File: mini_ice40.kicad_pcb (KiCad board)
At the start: 2 copper layers, 3 parts, among them P1 Pin_Header_Straight_1x18, P2 Pin_Header_Straight_1x18

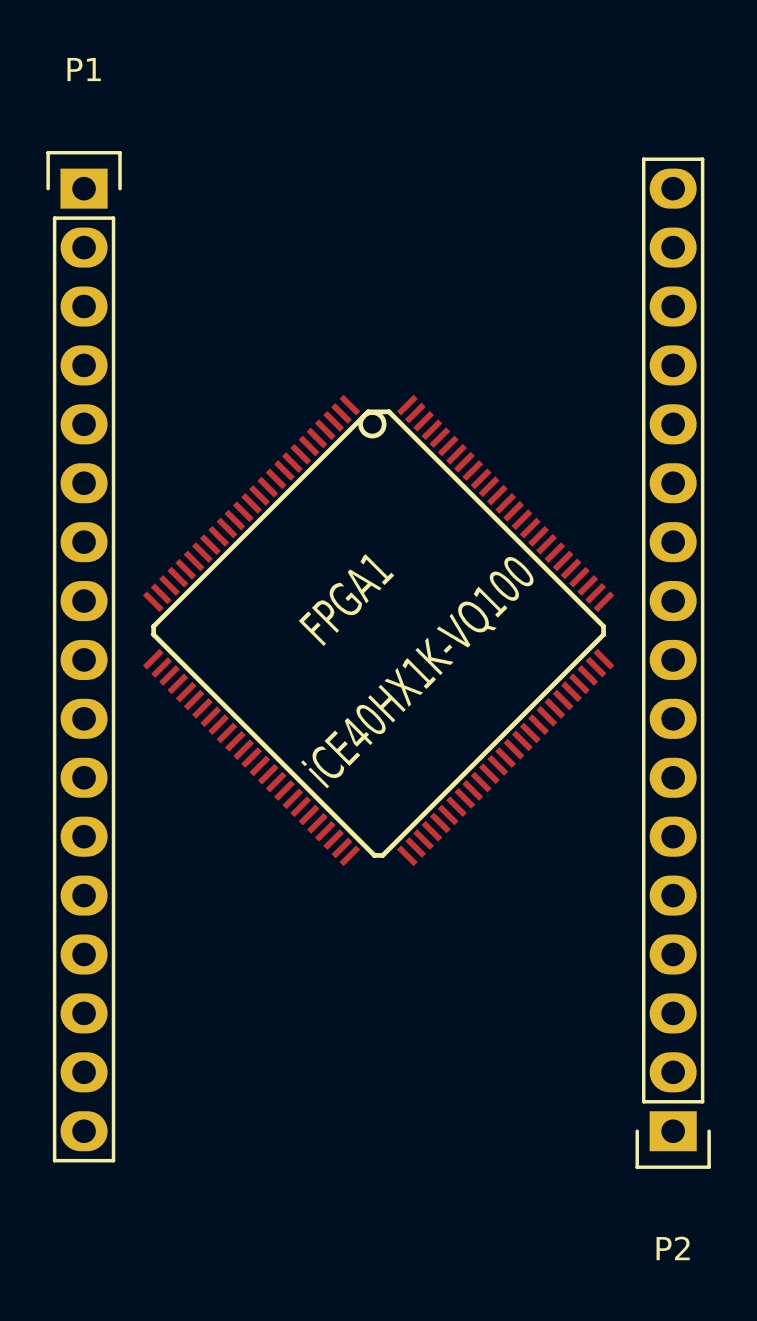
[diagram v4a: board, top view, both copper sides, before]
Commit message: ** 4-layer PCB design
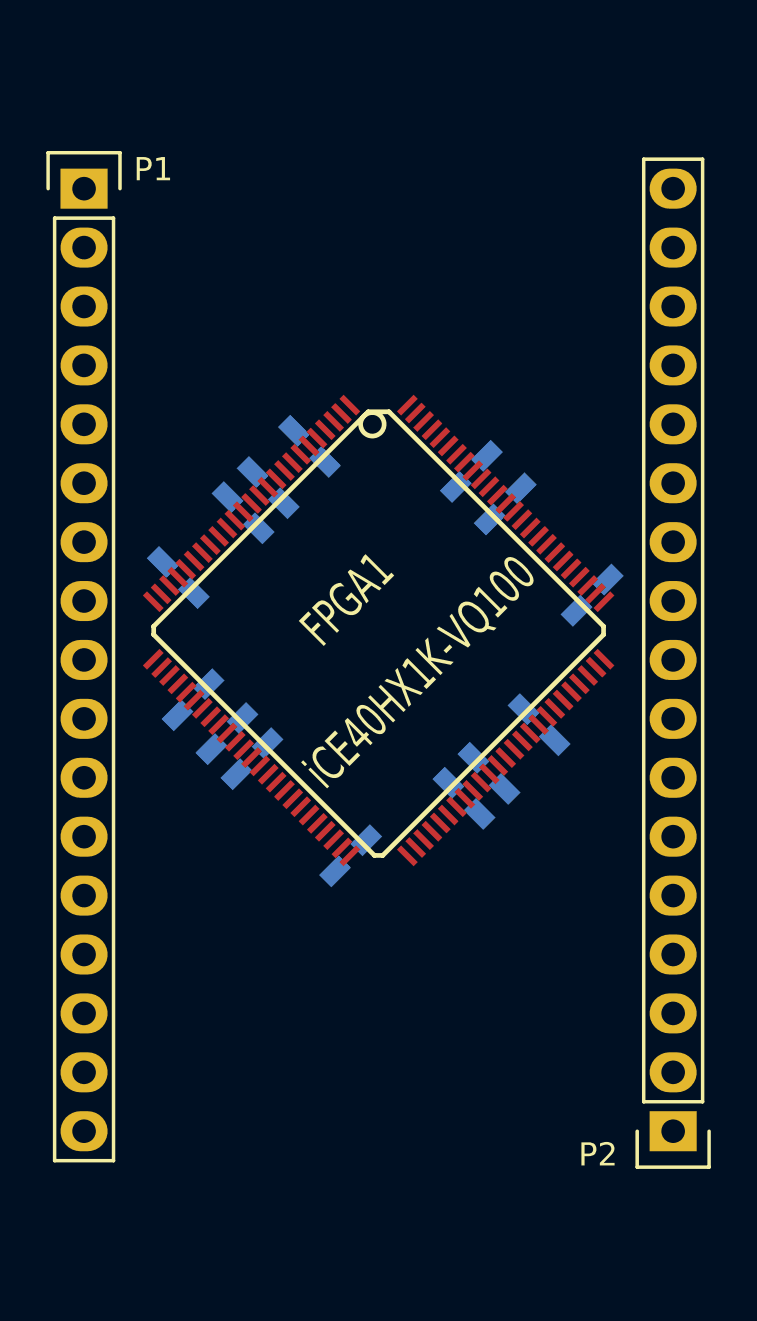
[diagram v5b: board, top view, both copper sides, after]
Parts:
- added C10: C_0603_HandSoldering, Capacitors_SMD:C_0603_HandSoldering, B.Cu at (22.5, 39.8)
- added C11: C_0603_HandSoldering, Capacitors_SMD:C_0603_HandSoldering, B.Cu at (26.7, 44.0)
- added C12: C_0603_HandSoldering, Capacitors_SMD:C_0603_HandSoldering, B.Cu at (31.6, 41.5)
- added C13: C_0603_HandSoldering, Capacitors_SMD:C_0603_HandSoldering, B.Cu at (34.9, 38.4)
- added C14: C_0603_HandSoldering, Capacitors_SMD:C_0603_HandSoldering, B.Cu at (33.4, 28.8)
- added C15: C_0603_HandSoldering, Capacitors_SMD:C_0603_HandSoldering, B.Cu at (31.9, 27.4)
- added C16: C_0603_HandSoldering, Capacitors_SMD:C_0603_HandSoldering, B.Cu at (23.2, 28.1)
- added C17: C_0603_HandSoldering, Capacitors_SMD:C_0603_HandSoldering, B.Cu at (21.4, 38.7)
- added C18: C_0603_HandSoldering, Capacitors_SMD:C_0603_HandSoldering, B.Cu at (32.7, 40.4)
- added C19: C_0603_HandSoldering, Capacitors_SMD:C_0603_HandSoldering, B.Cu at (37.1, 32.8)
- added C6: C_0603_HandSoldering, Capacitors_SMD:C_0603_HandSoldering, B.Cu at (25.0, 26.4)
- added C7: C_0603_HandSoldering, Capacitors_SMD:C_0603_HandSoldering, B.Cu at (22.1, 29.2)
- added C8: C_0603_HandSoldering, Capacitors_SMD:C_0603_HandSoldering, B.Cu at (19.3, 32.0)
- added C9: C_0603_HandSoldering, Capacitors_SMD:C_0603_HandSoldering, B.Cu at (19.9, 37.3)
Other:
- copper layers 2 -> 4
- net class Default: trace_width 0.25 -> 0.2; via_dia 0.6 -> 0.5; via_drill 0.4 -> 0.3

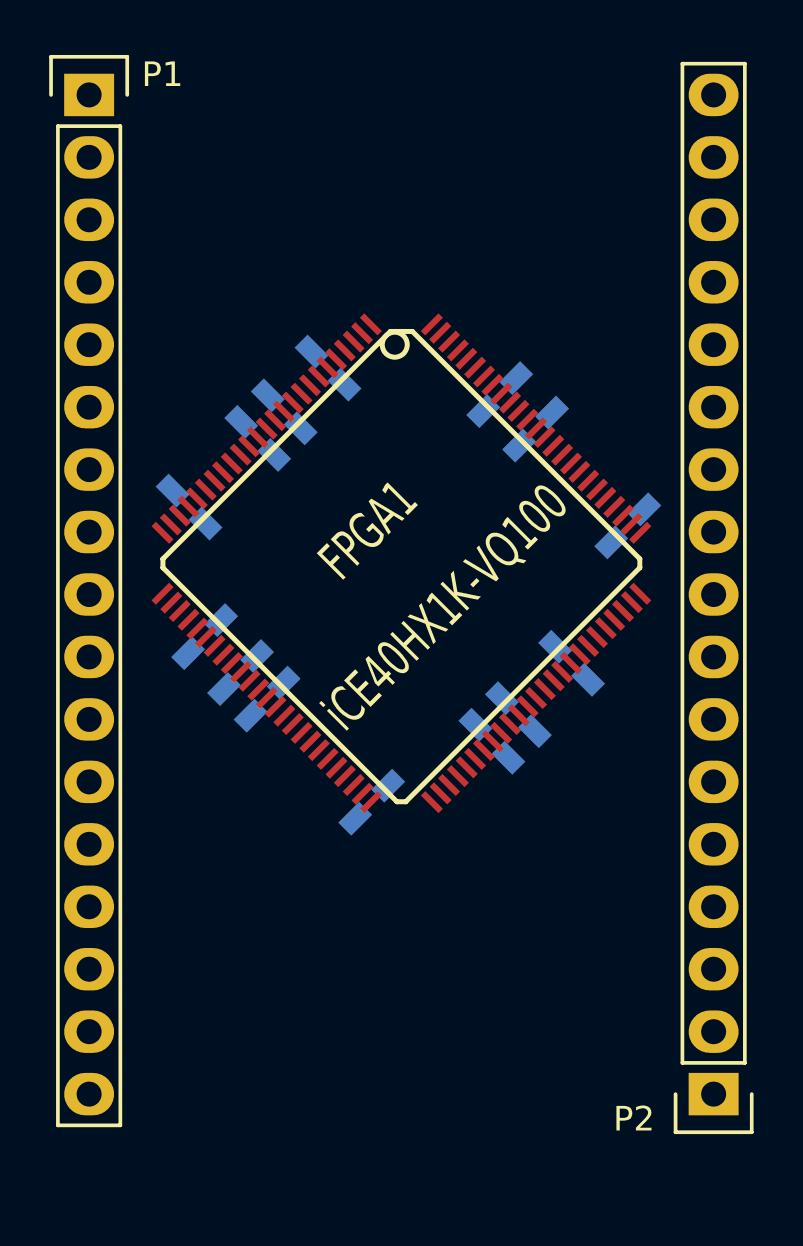
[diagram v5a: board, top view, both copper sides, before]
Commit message: ** 4-layer PCB sans GPIO
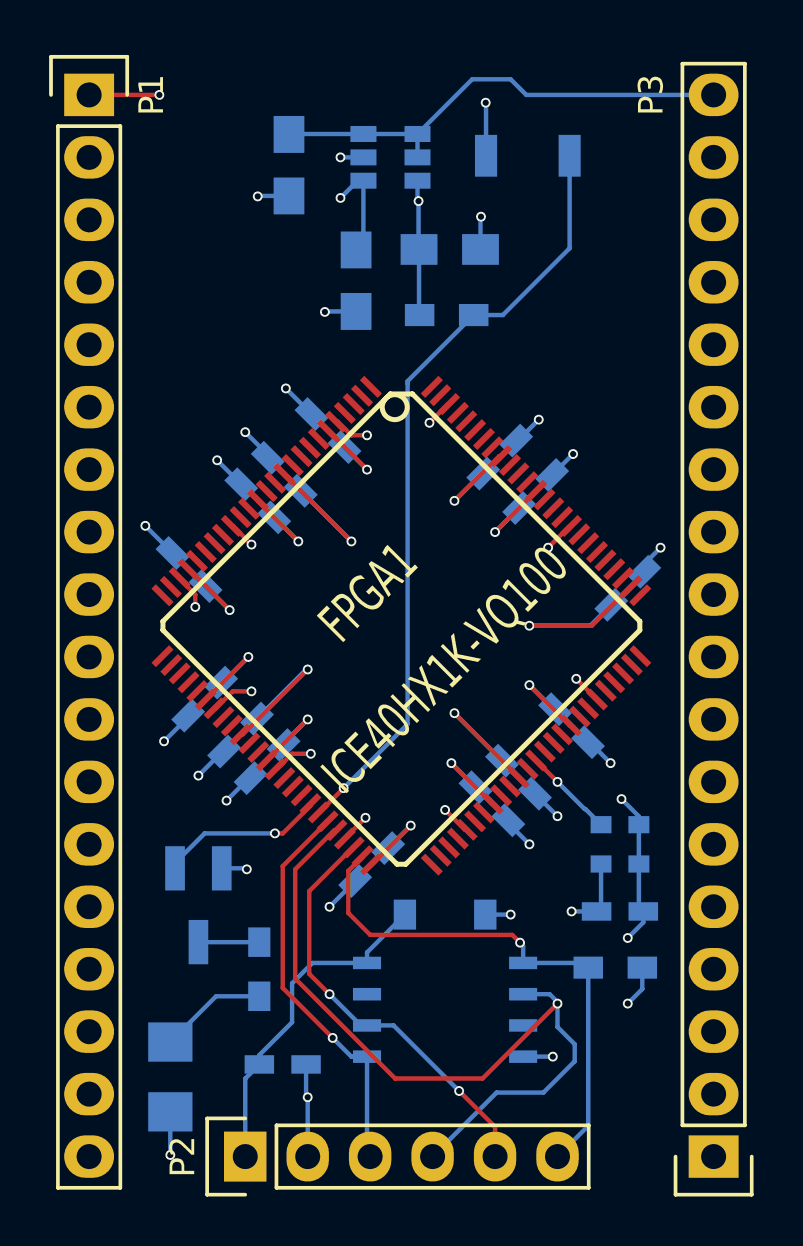
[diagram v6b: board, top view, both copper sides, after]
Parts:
- added C1: 1u, Capacitors_SMD:C_0805_HandSoldering, B.Cu at (23.4, 18.1)
- added C2: 1u, Capacitors_SMD:C_0805_HandSoldering, B.Cu at (26.1, 22.8)
- added C3: 1u, Capacitors_SMD:C_0805_HandSoldering, B.Cu at (29.9, 21.5)
- added C4: 0u1, Capacitors_SMD:C_0603_HandSoldering, B.Cu at (23.1, 54.7)
- added C5: 0u1, Capacitors_SMD:C_0603_HandSoldering, B.Cu at (36.8, 48.5)
- added D1: 1N4448WQ-7-F, Diodes_SMD:SOD-123, B.Cu at (29.7, 48.6)
- added DDONE1: SML-LX1206GC-TR1, LEDs:LED_1206, B.Cu at (18.5, 55.2)
- added OSC1: ASDMB-26MHZ-LC, mini_ice40:2MMx2MM5, B.Cu at (36.8, 45.7)
- added P3: CONN_01X18, Pin_Headers:Pin_Header_Straight_1x18, F.Cu at (40.6, 58.4)
- added Q1: 2N7002LT1G, TO_SOT_Packages_SMD:SOT-23_Handsoldering, B.Cu at (19.7, 48.2)
- added R1: 330, Resistors_SMD:R_0603_HandSoldering, B.Cu at (22.2, 50.8)
- added R2: 10K, Resistors_SMD:R_0603_HandSoldering, B.Cu at (29.8, 24.2)
- added R3: 10K, Resistors_SMD:R_0603_HandSoldering, B.Cu at (36.6, 50.7)
- added REG1: AP7312-1233W6-7, TO_SOT_Packages_SMD:SOT-23-6, B.Cu at (27.5, 17.8)
- added RST1: SW_PUSH, Buttons_Switches_SMD:SW_SPST_B3U-1000P, B.Cu at (33.1, 17.7)
- added SPI_FLASH1: AT25SF041-SSHD-B, SMD_Packages:SOIC-8-N, B.Cu at (29.7, 52.5)
- C10, C11, C12, C13, C14, C15, C16, C17, C18, C19, C6, C7, C8, C9: value C_0603_HandSoldering -> 0u1
- FPGA1: value iCE40HX1K-VQ100 -> ICE40HX1K-VQ100
- P1: value Pin_Header_Straight_1x18 -> CONN_01X18; footprint Pin_Headers:Pin_Header_Straight_1x17 -> Pin_Headers:Pin_Header_Straight_1x18
- P2: value Pin_Header_Straight_1x18 -> CONN_01X04; footprint Pin_Headers:Pin_Header_Straight_1x17 -> Pin_Headers:Pin_Header_Straight_1x06
- moved P2 19.2 mm to (21.6, 58.4), turned to 90 degrees
- moved C15 2.54 mm to (31.9, 30.0)
- moved C10 2.54 mm to (22.5, 42.4)
- moved C11 2.54 mm to (26.7, 46.5)
- moved C12 2.54 mm to (31.6, 44.1)
- moved C13 2.54 mm to (34.9, 40.9)
- moved C14 2.54 mm to (33.4, 31.4)
- moved C16 2.54 mm to (23.2, 30.7)
- moved C17 2.54 mm to (21.4, 41.3)
- moved C18 2.54 mm to (32.7, 43.0)
- moved C19 2.54 mm to (37.1, 35.3)
- moved C6 2.54 mm to (25.0, 28.9)
- moved C7 2.54 mm to (22.1, 31.8)
- moved C8 2.54 mm to (19.3, 34.5)
- moved C9 2.54 mm to (19.9, 39.8)
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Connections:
- C10 pad 1: (no net) -> +3V3
- C10 pad 2: (no net) -> GND
- C11 pad 1: (no net) -> +3V3
- C11 pad 2: (no net) -> GND
- C12 pad 1: (no net) -> +3V3
- C12 pad 2: (no net) -> GND
- C13 pad 1: (no net) -> +3V3
- C13 pad 2: (no net) -> GND
- C14 pad 1: (no net) -> +3V3
- C14 pad 2: (no net) -> GND
- C15 pad 1: (no net) -> +3V3
- C15 pad 2: (no net) -> GND
- C16 pad 1: (no net) -> +1V2
- C16 pad 2: (no net) -> GND
- C17 pad 1: (no net) -> +1V2
- C17 pad 2: (no net) -> GND
- C18 pad 1: (no net) -> +1V2
- C18 pad 2: (no net) -> GND
- C19 pad 1: (no net) -> +1V2
- C19 pad 2: (no net) -> GND
- C6 pad 1: (no net) -> +3V3
- C6 pad 2: (no net) -> GND
- C7 pad 1: (no net) -> +3V3
- C7 pad 2: (no net) -> GND
- C8 pad 1: (no net) -> +3V3
- C8 pad 2: (no net) -> GND
- C9 pad 1: (no net) -> +3V3
- C9 pad 2: (no net) -> GND
- FPGA1 pad 1: (no net) -> Net-(FPGA1-Pad1)
- FPGA1 pad 10: (no net) -> Net-(FPGA1-Pad10)
- FPGA1 pad 100: (no net) -> Net-(FPGA1-Pad100)
- FPGA1 pad 11: (no net) -> +1V2
- FPGA1 pad 12: (no net) -> Net-(FPGA1-Pad12)
- FPGA1 pad 13: (no net) -> Net-(FPGA1-Pad13)
- FPGA1 pad 14: (no net) -> +3V3
- FPGA1 pad 15: (no net) -> Net-(FPGA1-Pad15)
- FPGA1 pad 16: (no net) -> Net-(FPGA1-Pad16)
- FPGA1 pad 17: (no net) -> GND
- FPGA1 pad 18: (no net) -> Net-(FPGA1-Pad18)
- FPGA1 pad 19: (no net) -> Net-(FPGA1-Pad19)
- FPGA1 pad 2: (no net) -> Net-(FPGA1-Pad2)
- FPGA1 pad 20: (no net) -> Net-(FPGA1-Pad20)
- FPGA1 pad 21: (no net) -> Net-(FPGA1-Pad21)
- FPGA1 pad 22: (no net) -> +3V3
- FPGA1 pad 23: (no net) -> GND
- FPGA1 pad 24: (no net) -> Net-(FPGA1-Pad24)
- FPGA1 pad 25: (no net) -> Net-(FPGA1-Pad25)
- FPGA1 pad 26: (no net) -> Net-(FPGA1-Pad26)
- FPGA1 pad 27: (no net) -> Net-(FPGA1-Pad27)
- FPGA1 pad 28: (no net) -> Net-(FPGA1-Pad28)
- FPGA1 pad 29: (no net) -> Net-(FPGA1-Pad29)
- FPGA1 pad 3: (no net) -> Net-(FPGA1-Pad3)
- FPGA1 pad 30: (no net) -> Net-(FPGA1-Pad30)
- FPGA1 pad 31: (no net) -> +3V3
- FPGA1 pad 32: (no net) -> GND
- FPGA1 pad 33: (no net) -> Net-(FPGA1-Pad33)
- FPGA1 pad 34: (no net) -> Net-(FPGA1-Pad34)
- FPGA1 pad 35: (no net) -> +1V2
- FPGA1 pad 36: (no net) -> Net-(FPGA1-Pad36)
- FPGA1 pad 37: (no net) -> Net-(FPGA1-Pad37)
- FPGA1 pad 38: (no net) -> +3V3
- FPGA1 pad 39: (no net) -> GND
- FPGA1 pad 4: (no net) -> Net-(FPGA1-Pad4)
- FPGA1 pad 40: (no net) -> Net-(FPGA1-Pad40)
- FPGA1 pad 41: (no net) -> Net-(FPGA1-Pad41)
- FPGA1 pad 42: (no net) -> Net-(FPGA1-Pad42)
- FPGA1 pad 43: (no net) -> Net-(FPGA1-Pad43)
- FPGA1 pad 44: (no net) -> Net-(FPGA1-Pad44)
- FPGA1 pad 45: (no net) -> Net-(FPGA1-Pad45)
- FPGA1 pad 46: (no net) -> Net-(FPGA1-Pad46)
- FPGA1 pad 47: (no net) -> GND
- FPGA1 pad 48: (no net) -> Net-(FPGA1-Pad48)
- FPGA1 pad 49: (no net) -> Net-(FPGA1-Pad49)
- FPGA1 pad 5: (no net) -> GND
- FPGA1 pad 50: (no net) -> +3V3
- FPGA1 pad 51: (no net) -> Net-(FPGA1-Pad51)
- FPGA1 pad 52: (no net) -> Net-(FPGA1-Pad52)
- FPGA1 pad 53: (no net) -> Net-(FPGA1-Pad53)
- FPGA1 pad 54: (no net) -> Net-(FPGA1-Pad54)
- FPGA1 pad 55: (no net) -> GND
- FPGA1 pad 56: (no net) -> Net-(FPGA1-Pad56)
- FPGA1 pad 57: (no net) -> Net-(FPGA1-Pad57)
- FPGA1 pad 58: (no net) -> +3V3
- FPGA1 pad 59: (no net) -> Net-(FPGA1-Pad59)
- FPGA1 pad 6: (no net) -> +3V3
- FPGA1 pad 60: (no net) -> Net-(FPGA1-Pad60)
- FPGA1 pad 61: (no net) -> +1V2
- FPGA1 pad 62: (no net) -> Net-(FPGA1-Pad62)
- FPGA1 pad 63: (no net) -> Net-(FPGA1-Pad63)
- FPGA1 pad 64: (no net) -> Net-(FPGA1-Pad64)
- FPGA1 pad 65: (no net) -> Net-(FPGA1-Pad65)
- FPGA1 pad 66: (no net) -> Net-(FPGA1-Pad66)
- FPGA1 pad 67: (no net) -> +3V3
- FPGA1 pad 68: (no net) -> Net-(FPGA1-Pad68)
- FPGA1 pad 69: (no net) -> Net-(FPGA1-Pad69)
- FPGA1 pad 70: (no net) -> GND
- FPGA1 pad 71: (no net) -> Net-(FPGA1-Pad71)
- FPGA1 pad 72: (no net) -> Net-(FPGA1-Pad72)
- FPGA1 pad 73: (no net) -> Net-(FPGA1-Pad73)
- FPGA1 pad 74: (no net) -> Net-(FPGA1-Pad74)
- FPGA1 pad 75: (no net) -> Net-(FPGA1-Pad75)
- FPGA1 pad 76: (no net) -> Net-(FPGA1-Pad76)
- FPGA1 pad 77: (no net) -> +1V2
- FPGA1 pad 78: (no net) -> Net-(FPGA1-Pad78)
- FPGA1 pad 79: (no net) -> Net-(FPGA1-Pad79)
- FPGA1 pad 80: (no net) -> Net-(FPGA1-Pad80)
- FPGA1 pad 81: (no net) -> Net-(FPGA1-Pad81)
- FPGA1 pad 82: (no net) -> Net-(FPGA1-Pad82)
- FPGA1 pad 83: (no net) -> Net-(FPGA1-Pad83)
- FPGA1 pad 84: (no net) -> GND
- FPGA1 pad 85: (no net) -> Net-(FPGA1-Pad85)
- FPGA1 pad 86: (no net) -> Net-(FPGA1-Pad86)
- FPGA1 pad 87: (no net) -> Net-(FPGA1-Pad87)
- FPGA1 pad 88: (no net) -> +3V3
- FPGA1 pad 89: (no net) -> Net-(FPGA1-Pad89)
- FPGA1 pad 9: (no net) -> Net-(FPGA1-Pad9)
- FPGA1 pad 90: (no net) -> Net-(FPGA1-Pad90)
- FPGA1 pad 91: (no net) -> Net-(FPGA1-Pad91)
- FPGA1 pad 92: (no net) -> +3V3
- FPGA1 pad 93: (no net) -> Net-(FPGA1-Pad93)
- FPGA1 pad 94: (no net) -> Net-(FPGA1-Pad94)
- FPGA1 pad 95: (no net) -> Net-(FPGA1-Pad95)
- FPGA1 pad 96: (no net) -> Net-(FPGA1-Pad96)
- FPGA1 pad 97: (no net) -> Net-(FPGA1-Pad97)
- FPGA1 pad 98: (no net) -> GND
- FPGA1 pad 99: (no net) -> Net-(FPGA1-Pad99)
- P1 pad 1: (no net) -> GND
- P1 pad 10: (no net) -> Net-(FPGA1-Pad27)
- P1 pad 11: (no net) -> Net-(FPGA1-Pad28)
- P1 pad 12: (no net) -> Net-(FPGA1-Pad29)
- P1 pad 13: (no net) -> Net-(FPGA1-Pad30)
- P1 pad 14: (no net) -> Net-(FPGA1-Pad33)
- P1 pad 15: (no net) -> Net-(FPGA1-Pad37)
- P1 pad 16: (no net) -> Net-(FPGA1-Pad40)
- P1 pad 17: (no net) -> Net-(FPGA1-Pad41)
- P1 pad 2: (no net) -> Net-(FPGA1-Pad4)
- P1 pad 3: (no net) -> Net-(FPGA1-Pad9)
- P1 pad 4: (no net) -> Net-(FPGA1-Pad16)
- P1 pad 5: (no net) -> Net-(FPGA1-Pad18)
- P1 pad 6: (no net) -> Net-(FPGA1-Pad19)
- P1 pad 7: (no net) -> Net-(FPGA1-Pad20)
- P1 pad 8: (no net) -> Net-(FPGA1-Pad24)
- P1 pad 9: (no net) -> Net-(FPGA1-Pad25)
- P2 pad 1: (no net) -> Net-(C4-Pad1)
- P2 pad 2: (no net) -> GND
- P2 pad 3: (no net) -> Net-(FPGA1-Pad45)
- P2 pad 4: (no net) -> Net-(FPGA1-Pad46)
- P2 pad 5: (no net) -> Net-(FPGA1-Pad48)
- P2 pad 6: (no net) -> Net-(FPGA1-Pad49)
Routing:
- net GND: track 0.00 -> 55.4 mm, vias 0 -> 35
- net +3V3: track 0.00 -> 49.7 mm, vias 0 -> 15
- net +1V2: track 0.00 -> 34.1 mm, vias 0 -> 5
- net Net-(FPGA1-Pad46): track 0.00 -> 32.1 mm, vias 0 -> 1
- net Net-(FPGA1-Pad44): track 0.00 -> 31.6 mm, vias 0 -> 1
- net Net-(FPGA1-Pad49): track 0.00 -> 21.8 mm, vias 0 -> 1
- net VCC: track 0.00 -> 19.4 mm
- net Net-(FPGA1-Pad48): track 0.00 -> 17.2 mm, vias 0 -> 2
- net Net-(FPGA1-Pad45): track 0.00 -> 16.2 mm, vias 0 -> 1
- net Net-(C4-Pad1): track 0.00 -> 13.8 mm
- net Net-(FPGA1-Pad43): track 0.00 -> 6.75 mm, vias 0 -> 1
- net Net-(DDONE1-Pad1): track 0.00 -> 4.39 mm
- net Net-(FPGA1-Pad63): track 0.00 -> 3.72 mm, vias 0 -> 1
- net Net-(Q1-Pad3): track 0.00 -> 2.48 mm
- added copper zone on P.Cu, net +1V2
- added copper zone on P.Cu, net +3V3
- added copper zone on G.Cu, net GND
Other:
- net class Default: clearance 0.2 -> 0.18; trace_width 0.2 -> 0.18; via_dia 0.5 -> 0.4; via_drill 0.3 -> 0.25
- rule trace_clearance: 0.2 -> 0.18
- rule trace_min: 0.2 -> 0.18
- rule via_min_drill: 0.3 -> 0.25

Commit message: ** Finished 4-layer PCB layout
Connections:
- P3 pad 1: Net-(FPGA1-Pad51) -> Net-(FPGA1-Pad60)
- P3 pad 10: Net-(FPGA1-Pad85) -> Net-(FPGA1-Pad79)
- P3 pad 11: Net-(FPGA1-Pad86) -> Net-(FPGA1-Pad80)
- P3 pad 12: Net-(FPGA1-Pad90) -> Net-(FPGA1-Pad81)
- P3 pad 13: Net-(FPGA1-Pad95) -> Net-(FPGA1-Pad82)
- P3 pad 14: Net-(FPGA1-Pad96) -> Net-(FPGA1-Pad83)
- P3 pad 15: Net-(FPGA1-Pad97) -> Net-(FPGA1-Pad85)
- P3 pad 16: Net-(FPGA1-Pad99) -> Net-(FPGA1-Pad86)
- P3 pad 17: Net-(FPGA1-Pad100) -> Net-(FPGA1-Pad90)
- P3 pad 2: Net-(FPGA1-Pad52) -> Net-(FPGA1-Pad62)
- P3 pad 3: Net-(FPGA1-Pad53) -> Net-(FPGA1-Pad64)
- P3 pad 4: Net-(FPGA1-Pad54) -> Net-(FPGA1-Pad65)
- P3 pad 5: Net-(FPGA1-Pad56) -> Net-(FPGA1-Pad69)
- P3 pad 6: Net-(FPGA1-Pad57) -> Net-(FPGA1-Pad71)
- P3 pad 7: Net-(FPGA1-Pad59) -> Net-(FPGA1-Pad72)
- P3 pad 8: Net-(FPGA1-Pad60) -> Net-(FPGA1-Pad73)
- P3 pad 9: Net-(FPGA1-Pad62) -> Net-(FPGA1-Pad74)
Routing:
- net Net-(FPGA1-Pad60): track 0.00 -> 18.5 mm
- net Net-(FPGA1-Pad42): track 0.00 -> 18.3 mm
- net Net-(FPGA1-Pad62): track 0.00 -> 16.7 mm
- net Net-(FPGA1-Pad90): track 0.00 -> 16.2 mm
- net Net-(FPGA1-Pad41): track 0.00 -> 15.9 mm
- net Net-(FPGA1-Pad4): track 0.00 -> 14.7 mm
- net Net-(FPGA1-Pad86): track 0.00 -> 14.4 mm
- net Net-(FPGA1-Pad64): track 0.00 -> 14.2 mm
- net Net-(FPGA1-Pad40): track 0.00 -> 13.6 mm
- net Net-(FPGA1-Pad9): track 0.00 -> 13.2 mm
- net Net-(FPGA1-Pad16): track 0.00 -> 12.1 mm
- net Net-(FPGA1-Pad85): track 0.00 -> 12.1 mm
- net Net-(FPGA1-Pad65): track 0.00 -> 11.9 mm
- net Net-(FPGA1-Pad37): track 0.00 -> 11.7 mm
- net Net-(FPGA1-Pad69): track 0.00 -> 10.2 mm
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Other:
- net class Power added: clearance 0.13, trace_width 0.25, via_dia 0.4, via_drill 0.25
